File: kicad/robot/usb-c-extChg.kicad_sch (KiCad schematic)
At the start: 11 parts, among them J1 USBC_Receptacle_SMD_RA

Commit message: WARNING Major BOM cleanup
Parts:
- J1: DESCRIPTION_ CON USB3.1 TID TYPE-C Female SMD R/A -> (none); MANUFACTURER 1 Amphenol Commercial Products -> (none); MANUFACTURER PART NUMBER 1 12401610E4#2A -> (none); MCHP-ID CON1809 -> (none); Manufacturer (none) -> Amphenol Commercial Products; Part Number (none) -> 12401610E4#2A
- TP10: value CC2 -> TP5002
- TP11: value VBUS -> TP5002
- TP7: value D- -> TP5002
- TP8: value D+ -> TP5002
- TP9: value CC1 -> TP5002
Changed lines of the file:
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@@
       (effects (font (size 1.27 1.27)) (justify left))
     )
-    (property "Value" "D+" (id 1) (at 162.56 124.46 90)
+    (property "Value" "TP5002" (id 1) (at 162.56 124.46 90)
       (effects (font (size 1.27 1.27)) (justify left))
     )
@@
     )
     (property "Datasheet" "~" (id 3) (at 157.48 129.54 0)
+      (effects (font (size 1.27 1.27)) hide)
+    )
+    (property "Description" "ExtC_D+" (id 4) (at 157.48 124.46 0)
       (effects (font (size 1.27 1.27)) hide)
     )
@@
       (effects (font (size 1.27 1.27)) (justify left))
     )
-    (property "Value" "CC1" (id 1) (at 177.8 127 0)
+    (property "Value" "TP5002" (id 1) (at 177.8 127 0)
       (effects (font (size 1.27 1.27)) (justify left))
     )
@@
     )
     (property "Datasheet" "~" (id 3) (at 180.34 129.54 0)
+      (effects (font (size 1.27 1.27)) hide)
+    )
+    (property "Description" "ExtC_CC1" (id 4) (at 175.26 129.54 0)
       (effects (font (size 1.27 1.27)) hide)
     )
@@
       (effects (font (size 1.27 1.27)) (justify left))
     )
-    (property "Value" "VBUS" (id 1) (at 195.58 68.58 0)
+    (property "Value" "TP5002" (id 1) (at 195.58 68.58 0)
       (effects (font (size 1.27 1.27)) (justify left))
     )
@@
     )
     (property "Datasheet" "~" (id 3) (at 198.12 71.12 0)
+      (effects (font (size 1.27 1.27)) hide)
+    )
+    (property "Description" "ExtC_VBUS" (id 4) (at 193.04 71.12 0)
       (effects (font (size 1.27 1.27)) hide)
     )
@@
       (effects (font (size 1.27 1.27)) hide)
     )
-    (property "MCHP-ID" "CON1809" (id 4) (at 111.252 62.23 0)
+    (property "MCHP-ID" "" (id 4) (at 111.252 62.23 0)
       (effects (font (size 1.27 1.27)) (justify left bottom) hide)
     )
@@
       (effects (font (size 1.27 1.27)) (justify left bottom) hide)
     )
-    (property "DESCRIPTION_" "CON USB3.1 TID TYPE-C Female SMD R/A" (id 8) (at 111.252 62.23 0)
-      (effects (font (size 1.27 1.27)) (justify left bottom) hide)
-    )
     (property "STATUS" "MCL Design" (id 9) (at 111.252 62.23 0)
       (effects (font (size 1.27 1.27)) (justify left bottom) hide)
@@
       (effects (font (size 1.27 1.27)) (justify left bottom) hide)
     )
-    (property "MANUFACTURER 1" "Amphenol Commercial Products" (id 26) (at 111.252 62.23 0)
-      (effects (font (size 1.27 1.27)) (justify left bottom) hide)
-    )
-    (property "MANUFACTURER PART NUMBER 1" "12401610E4#2A" (id 27) (at 111.252 62.23 0)
+    (property "MANUFACTURER 1" "" (id 26) (at 111.252 62.23 0)
+      (effects (font (size 1.27 1.27)) (justify left bottom) hide)
+    )
+    (property "MANUFACTURER PART NUMBER 1" "" (id 27) (at 111.252 62.23 0)
       (effects (font (size 1.27 1.27)) (justify left bottom) hide)
     )
@@
     (property "BOM NOTES" "" (id 33) (at 111.252 62.23 0)
       (effects (font (size 1.27 1.27)) (justify left bottom) hide)
+    )
+    (property "Description" "CON USB3.1 TID TYPE-C Female SMD R/A" (id 34) (at 134.62 62.23 0)
+      (effects (font (size 1.27 1.27)) hide)
+    )
+    (property "Manufacturer" "Amphenol Commercial Products" (id 35) (at 134.62 62.23 0)
+      (effects (font (size 1.27 1.27)) hide)
+    )
+    (property "Part Number" "12401610E4#2A" (id 36) (at 134.62 62.23 0)
+      (effects (font (size 1.27 1.27)) hide)
     )
     (pin "25")
@@
       (effects (font (size 1.27 1.27)) (justify left))
     )
-    (property "Value" "D-" (id 1) (at 152.4 123.1899 90)
+    (property "Value" "TP5002" (id 1) (at 152.4 123.1899 90)
       (effects (font (size 1.27 1.27)) (justify left))
     )
@@
       (effects (font (size 1.27 1.27)) hide)
     )
+    (property "Description" "ExtC_D-" (id 4) (at 147.32 121.92 0)
+      (effects (font (size 1.27 1.27)) hide)
+    )
     (pin "1")
   )
@@
       (effects (font (size 1.27 1.27)) (justify right))
     )
-    (property "Value" "CC2" (id 1) (at 177.8 137.16 0)
+    (property "Value" "TP5002" (id 1) (at 177.8 137.16 0)
       (effects (font (size 1.27 1.27)) (justify right))
     )
@@
       (effects (font (size 1.27 1.27)) hide)
     )
+    (property "Description" "ExtC_CC2" (id 4) (at 175.26 132.08 0)
+      (effects (font (size 1.27 1.27)) hide)
+    )

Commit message: WARNING more BOM batch edits
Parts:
- TP10, TP11, TP7, TP8, TP9: Manufacturer (none) -> Keystone Electronics; Part Number (none) -> 5002
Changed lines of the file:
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@@
+      (effects (font (size 1.27 1.27)) hide)
+    )
+    (property "Manufacturer" "Keystone Electronics" (id 5) (at 157.48 124.46 0)
+      (effects (font (size 1.27 1.27)) hide)
+    )
+    (property "Part Number" "5002" (id 6) (at 157.48 124.46 0)
       (effects (font (size 1.27 1.27)) hide)
     )
@@
       (effects (font (size 1.27 1.27)) hide)
     )
+    (property "Manufacturer" "Keystone Electronics" (id 5) (at 175.26 129.54 0)
+      (effects (font (size 1.27 1.27)) hide)
+    )
+    (property "Part Number" "5002" (id 6) (at 175.26 129.54 0)
+      (effects (font (size 1.27 1.27)) hide)
+    )
     (pin "1")
   )
@@
     )
     (property "Description" "ExtC_VBUS" (id 4) (at 193.04 71.12 0)
+      (effects (font (size 1.27 1.27)) hide)
+    )
+    (property "Manufacturer" "Keystone Electronics" (id 5) (at 193.04 71.12 0)
+      (effects (font (size 1.27 1.27)) hide)
+    )
+    (property "Part Number" "5002" (id 6) (at 193.04 71.12 0)
       (effects (font (size 1.27 1.27)) hide)
     )
@@
       (effects (font (size 1.27 1.27)) hide)
     )
+    (property "Manufacturer" "Keystone Electronics" (id 5) (at 147.32 121.92 0)
+      (effects (font (size 1.27 1.27)) hide)
+    )
+    (property "Part Number" "5002" (id 6) (at 147.32 121.92 0)
+      (effects (font (size 1.27 1.27)) hide)
+    )
     (pin "1")
   )
@@
       (effects (font (size 1.27 1.27)) hide)
     )
+    (property "Manufacturer" "Keystone Electronics" (id 5) (at 175.26 132.08 0)
+      (effects (font (size 1.27 1.27)) hide)
+    )
+    (property "Part Number" "5002" (id 6) (at 175.26 132.08 0)
+      (effects (font (size 1.27 1.27)) hide)
+    )

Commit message: Batch BOM edits adding manufactuer and part numbers only
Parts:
- D2: Manufacturer (none) -> Nexperia
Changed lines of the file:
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@@
+      (effects (font (size 1.27 1.27)) hide)
+    )
+    (property "Manufacturer" "Nexperia" (id 6) (at 167.64 81.28 0)
       (effects (font (size 1.27 1.27)) hide)
     )

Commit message: bulk BOM edits. Mainly dealing with cap voltage ratings and part selection
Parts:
- C18, C19: Manufacturer (none) -> Murata; Part Number (none) -> GRM1555C1H270JA01J
- C20: Manufacturer (none) -> Samsung; Part Number (none) -> CL21B225KBYNNNE
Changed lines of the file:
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@@
     )
     (property "Description" "35V" (id 4) (at 190.5 82.55 0))
+    (property "Manufacturer" "Samsung" (id 5) (at 185.42 78.74 0)
+      (effects (font (size 1.27 1.27)) hide)
+    )
+    (property "Part Number" "CL21B225KBYNNNE" (id 6) (at 185.42 78.74 0)
+      (effects (font (size 1.27 1.27)) hide)
+    )
     (pin "1")
     (pin "2")
@@
     )
     (property "Description" "50V" (id 4) (at 170.18 142.24 0)
+      (effects (font (size 1.27 1.27)) hide)
+    )
+    (property "Manufacturer" "Murata" (id 5) (at 170.18 142.24 0)
+      (effects (font (size 1.27 1.27)) hide)
+    )
+    (property "Part Number" "GRM1555C1H270JA01J" (id 6) (at 170.18 142.24 0)
       (effects (font (size 1.27 1.27)) hide)
     )
@@
       (effects (font (size 1.27 1.27)) hide)
     )
+    (property "Manufacturer" "Murata" (id 5) (at 157.48 142.24 0)
+      (effects (font (size 1.27 1.27)) hide)
+    )
+    (property "Part Number" "GRM1555C1H270JA01J" (id 6) (at 157.48 142.24 0)
+      (effects (font (size 1.27 1.27)) hide)
+    )

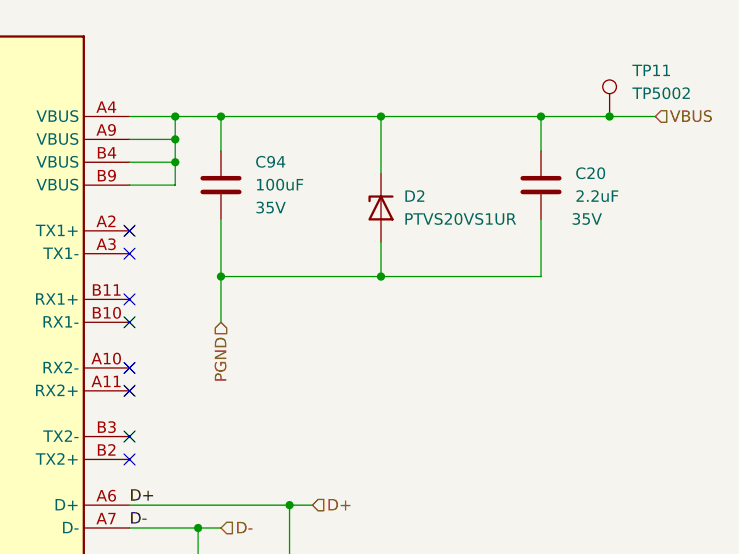
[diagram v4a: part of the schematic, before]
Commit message: Updating bulk caps on USB VBUS
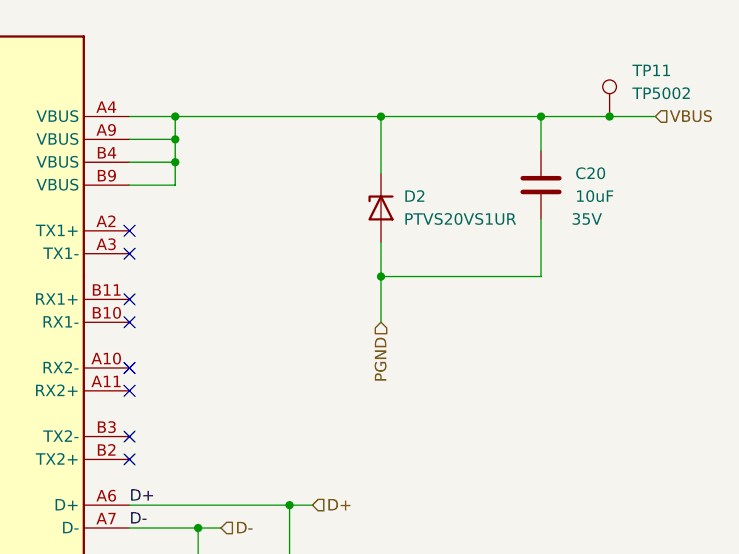
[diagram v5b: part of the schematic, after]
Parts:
- removed C94: 100uF, Capacitor_SMD:C_1210_3225Metric, symbol Device:C
- C20: value 2.2uF -> 10uF; Manufacturer Samsung -> (none); Part Number CL21B225KBYNNNE -> (none)
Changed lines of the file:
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@@
   (junction (at 147.32 116.84) (diameter 0) (color 0 0 0 0)
   )
-  (junction (at 149.86 71.12) (diameter 0) (color 0 0 0 0)
-  )
   (junction (at 147.32 121.92) (diameter 0) (color 0 0 0 0)
   )
@@
   )
   (junction (at 157.48 129.54) (diameter 0) (color 0 0 0 0)
-  )
-  (junction (at 149.86 88.9) (diameter 0) (color 0 0 0 0)
   )
   (junction (at 144.78 73.66) (diameter 0) (color 0 0 0 0)
@@
     (stroke (width 0.254) (type default) (color 0 0 0 0))
   )
-  (wire (pts (xy 144.78 71.12) (xy 149.86 71.12))
+  (wire (pts (xy 144.78 71.12) (xy 167.64 71.12))
     (stroke (width 0.254) (type default) (color 0 0 0 0))
   )
@@
     (stroke (width 0.254) (type default) (color 0 0 0 0))
   )
-  (wire (pts (xy 149.86 71.12) (xy 149.86 74.93))
-    (stroke (width 0) (type default) (color 0 0 0 0))
-  )
   (wire (pts (xy 139.7 76.2) (xy 144.78 76.2))
     (stroke (width 0.254) (type default) (color 0 0 0 0))
@@
     (stroke (width 0) (type default) (color 0 0 0 0))
   )
-  (wire (pts (xy 167.64 88.9) (xy 149.86 88.9))
-    (stroke (width 0) (type default) (color 0 0 0 0))
-  )
   (wire (pts (xy 109.22 127) (xy 109.22 129.54))
     (stroke (width 0.254) (type default) (color 0 0 0 0))
@@
     (stroke (width 0.254) (type default) (color 0 0 0 0))
   )
-  (wire (pts (xy 149.86 93.98) (xy 149.86 88.9))
+  (wire (pts (xy 167.64 93.98) (xy 167.64 88.9))
     (stroke (width 0) (type default) (color 0 0 0 0))
   )
   (wire (pts (xy 109.22 134.62) (xy 109.22 137.16))
     (stroke (width 0.254) (type default) (color 0 0 0 0))
-  )
-  (wire (pts (xy 149.86 71.12) (xy 167.64 71.12))
-    (stroke (width 0.254) (type default) (color 0 0 0 0))
-  )
-  (wire (pts (xy 149.86 82.55) (xy 149.86 88.9))
-    (stroke (width 0) (type default) (color 0 0 0 0))
   )
   (wire (pts (xy 185.42 71.12) (xy 185.42 74.93))
@@
     (effects (font (size 1.27 1.27)) (justify left))
   )
-  (hierarchical_label "PGND" (shape input) (at 149.86 93.98 270)
+  (hierarchical_label "PGND" (shape input) (at 167.64 93.98 270)
     (effects (font (size 1.27 1.27)) (justify right))
   )
@@
       (effects (font (size 1.27 1.27)) (justify left))
     )
-    (property "Value" "2.2uF" (id 1) (at 189.23 80.0099 0)
+    (property "Value" "10uF" (id 1) (at 189.23 80.0099 0)
       (effects (font (size 1.27 1.27)) (justify left))
     )
@@
     )
     (property "Description" "35V" (id 4) (at 190.5 82.55 0))
-    (property "Manufacturer" "Samsung" (id 5) (at 185.42 78.74 0)
-      (effects (font (size 1.27 1.27)) hide)
-    )
-    (property "Part Number" "CL21B225KBYNNNE" (id 6) (at 185.42 78.74 0)
-      (effects (font (size 1.27 1.27)) hide)
-    )
     (pin "1")
     (pin "2")
@@
     )
     (pin "1")
-    (pin "2")
-  )
-  (symbol (lib_id "Device:C") (at 149.86 78.74 0) (unit 1)
-    (in_bom yes) (on_board yes) (fields_autoplaced)
-    (property "Reference" "C94" (id 0) (at 153.67 76.1999 0)
-      (effects (font (size 1.27 1.27)) (justify left))
-    )
-    (property "Value" "100uF" (id 1) (at 153.67 78.7399 0)
-      (effects (font (size 1.27 1.27)) (justify left))
-    )
-    (property "Footprint" "Capacitor_SMD:C_1210_3225Metric" (id 2) (at 150.8252 82.55 0)
-      (effects (font (size 1.27 1.27)) hide)
-    )
-    (property "Datasheet" "~" (id 3) (at 149.86 78.74 0)
-      (effects (font (size 1.27 1.27)) hide)
-    )
-    (property "Description" "35V" (id 4) (at 153.67 81.2799 0)
-      (effects (font (size 1.27 1.27)) (justify left))
-    )
-    (pin "1")

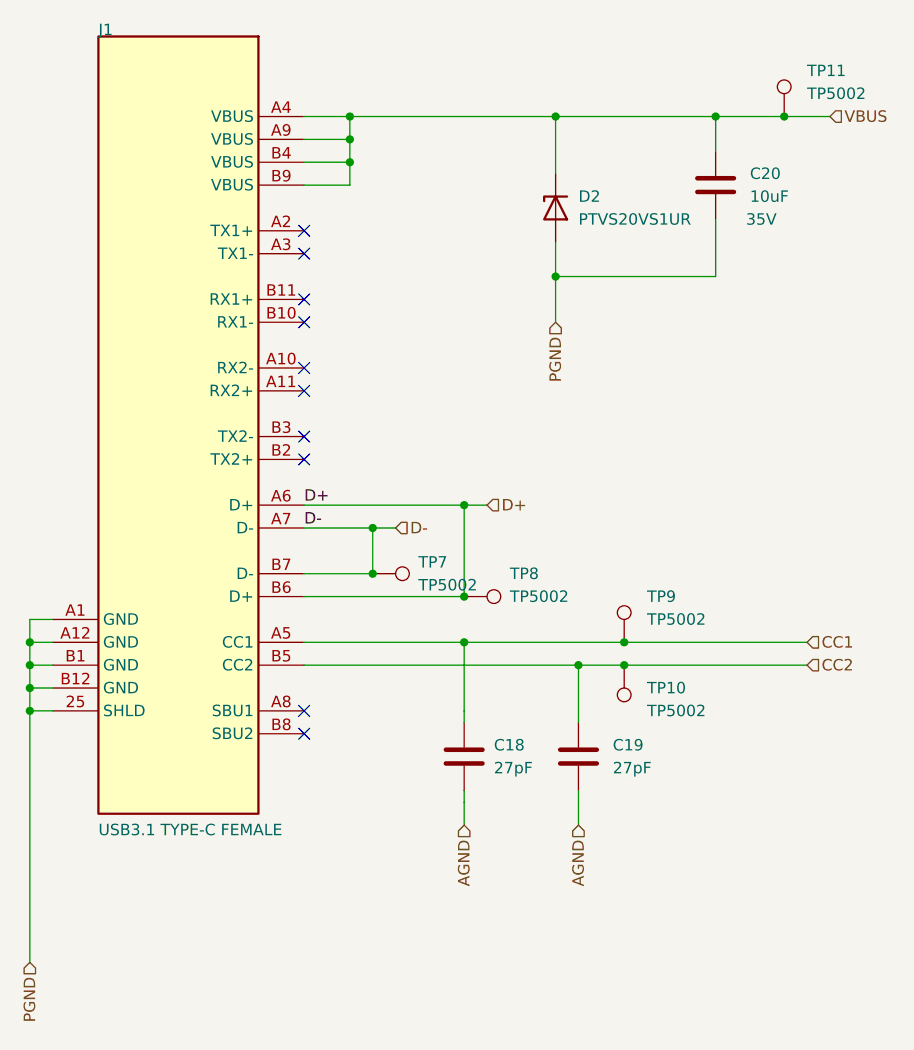
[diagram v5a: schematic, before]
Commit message: Bulk capacitor field edits
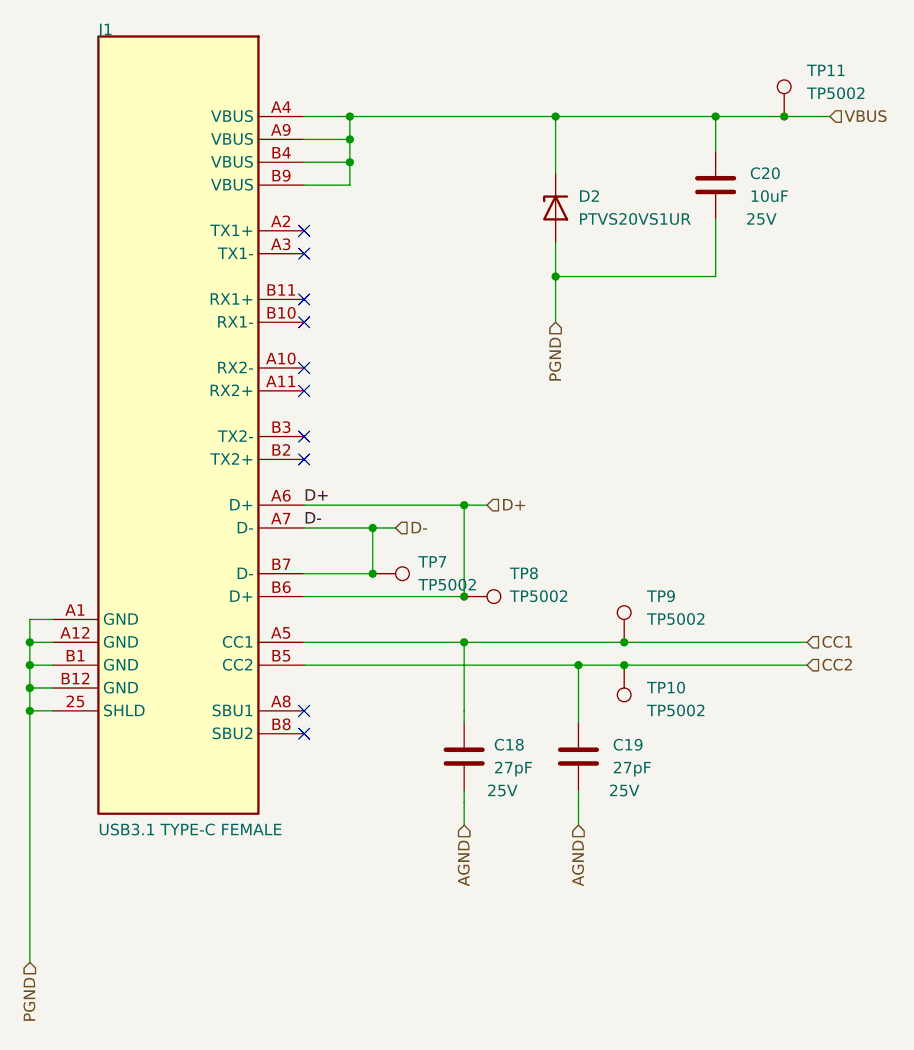
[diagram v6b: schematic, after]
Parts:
- C18, C19: Manufacturer Murata -> (none); Part Number GRM1555C1H270JA01J -> (none)
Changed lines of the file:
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@@
       (effects (font (size 1.27 1.27)) hide)
     )
-    (property "Description" "35V" (id 4) (at 190.5 82.55 0))
+    (property "Description" "25V" (id 4) (at 190.5 82.55 0))
     (pin "1")
     (pin "2")
@@
   )
   (symbol (lib_id "Device:C") (at 170.18 142.24 0) (unit 1)
-    (in_bom yes) (on_board yes) (fields_autoplaced)
+    (in_bom yes) (on_board yes)
     (property "Reference" "C19" (id 0) (at 173.99 140.9699 0)
       (effects (font (size 1.27 1.27)) (justify left))
@@
       (effects (font (size 1.27 1.27)) hide)
     )
-    (property "Description" "50V" (id 4) (at 170.18 142.24 0)
-      (effects (font (size 1.27 1.27)) hide)
-    )
-    (property "Manufacturer" "Murata" (id 5) (at 170.18 142.24 0)
-      (effects (font (size 1.27 1.27)) hide)
-    )
-    (property "Part Number" "GRM1555C1H270JA01J" (id 6) (at 170.18 142.24 0)
-      (effects (font (size 1.27 1.27)) hide)
-    )
+    (property "Description" "25V" (id 4) (at 175.26 146.05 0))
     (pin "1")
     (pin "2")
@@
       (effects (font (size 1.27 1.27)) hide)
     )
-    (property "Description" "50V" (id 4) (at 157.48 142.24 0)
-      (effects (font (size 1.27 1.27)) hide)
-    )
-    (property "Manufacturer" "Murata" (id 5) (at 157.48 142.24 0)
-      (effects (font (size 1.27 1.27)) hide)
-    )
-    (property "Part Number" "GRM1555C1H270JA01J" (id 6) (at 157.48 142.24 0)
-      (effects (font (size 1.27 1.27)) hide)
-    )
-    (pin "1")
+    (property "Description" "25V" (id 4) (at 160.02 146.05 0)
+      (effects (font (size 1.27 1.27)) (justify left))
+    )
+    (pin "1")

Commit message: bulk footprint updates to capacitors
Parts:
- C20: footprint Capacitor_SMD:C_0805_2012Metric -> Capacitor_SMD:C_0603_1608Metric
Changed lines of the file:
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@@
       (effects (font (size 1.27 1.27)) (justify left))
     )
-    (property "Footprint" "Capacitor_SMD:C_0805_2012Metric" (id 2) (at 186.3852 82.55 0)
+    (property "Footprint" "Capacitor_SMD:C_0603_1608Metric" (id 2) (at 186.3852 82.55 0)
       (effects (font (size 1.27 1.27)) hide)
     )
